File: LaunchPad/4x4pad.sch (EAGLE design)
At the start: 17 parts

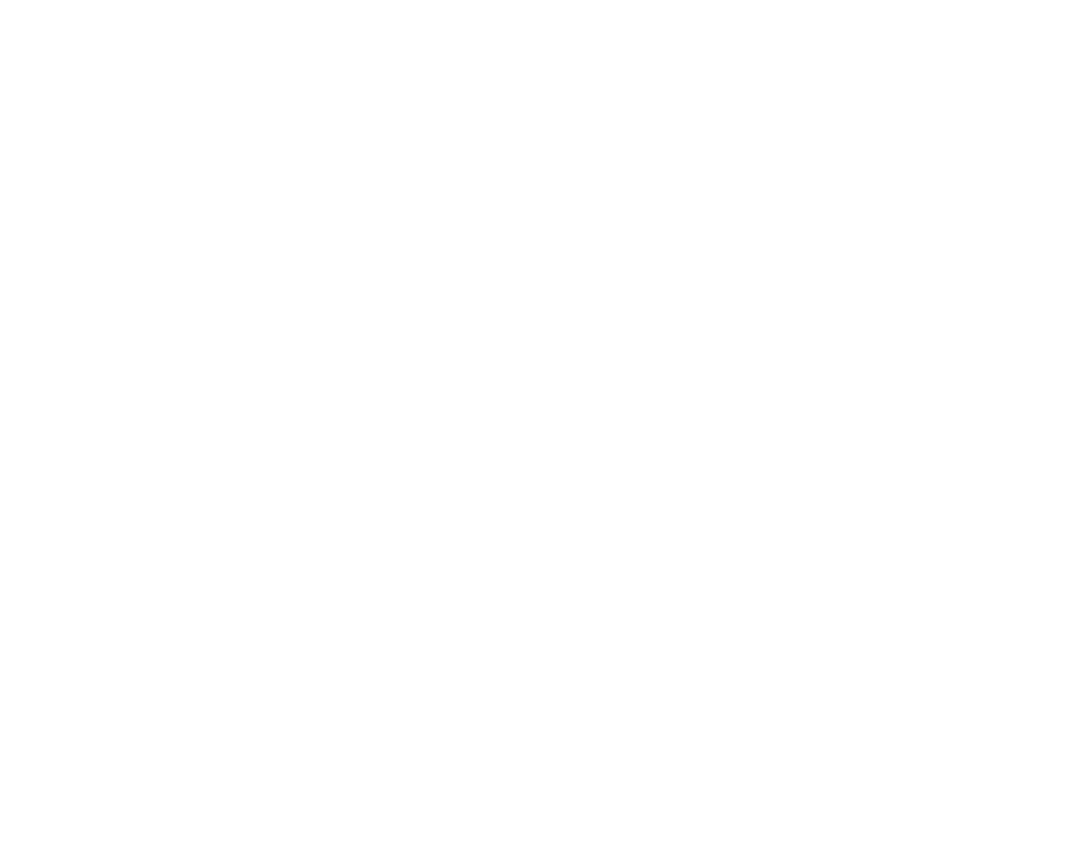
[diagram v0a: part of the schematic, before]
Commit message: Restarted 4x4 board, still need vertical button jumpoers, button connection
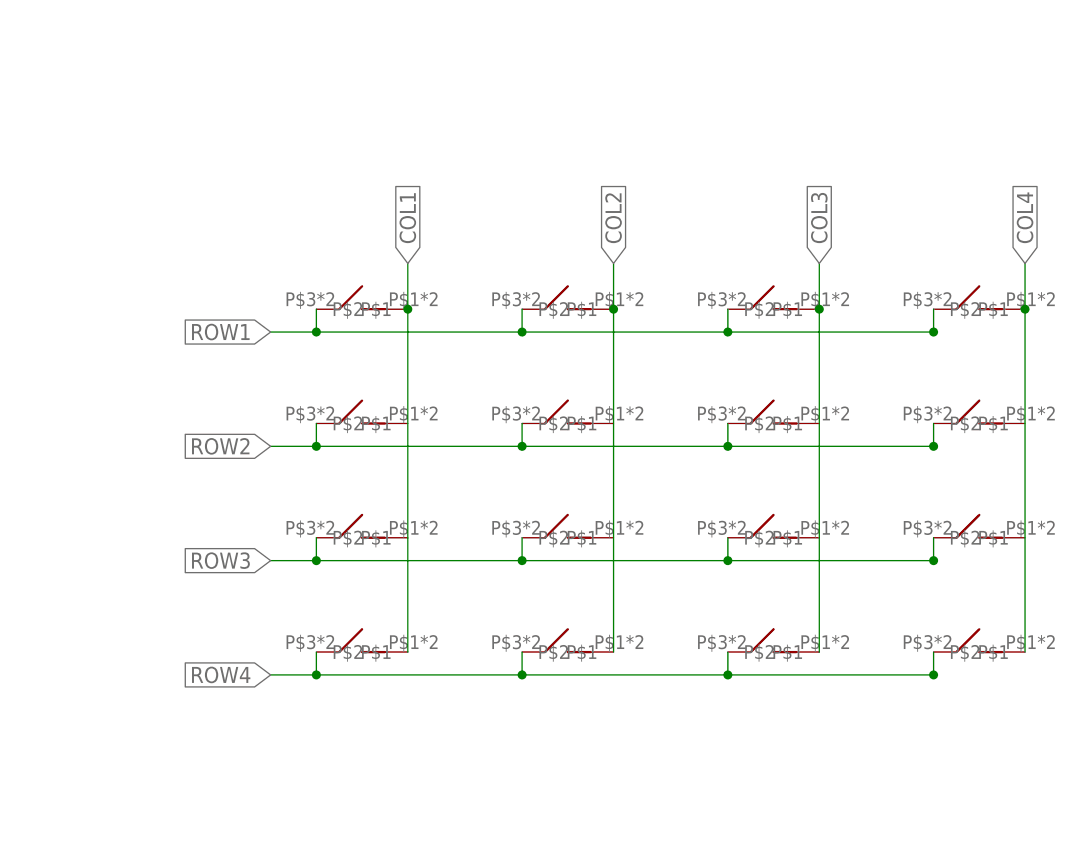
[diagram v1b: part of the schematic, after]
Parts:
- added U$18, U$19, U$20, U$21, U$22, U$23, U$24, U$25, U$26, U$27, U$28, U$29, U$30, U$31, U$32, U$33: SOFT-TACTILE-PUSHBUTTON, launchpadParts:SOFT-TACTILE-PUSHBUTTON
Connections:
- net +5V renamed N$36
- net GND renamed N$37
- new net COL1: U$18.P$2, U$30.P$2
- new net COL2: U$19.P$2, U$31.P$2
- new net COL3: U$20.P$2, U$32.P$2
- new net COL4: U$21.P$2, U$33.P$2
- new net ROW1: U$18.P$1, U$19.P$1, U$20.P$1, U$21.P$1
- new net ROW2: U$22.P$1, U$23.P$1, U$24.P$1, U$25.P$1
- new net ROW3: U$26.P$1, U$27.P$1, U$28.P$1, U$29.P$1
- new net ROW4: U$30.P$1, U$31.P$1, U$32.P$1, U$33.P$1
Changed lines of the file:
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@@
 <part name="P+16" library="supply1" library_urn="urn:adsk.eagle:library:371" deviceset="+5V" device=""/>
 <part name="P+17" library="supply1" library_urn="urn:adsk.eagle:library:371" deviceset="+5V" device=""/>
+<part name="U$18" library="launchpadParts" deviceset="SOFT-TACTILE-PUSHBUTTON" device=""/>
+<part name="U$19" library="launchpadParts" deviceset="SOFT-TACTILE-PUSHBUTTON" device=""/>
+<part name="U$20" library="launchpadParts" deviceset="SOFT-TACTILE-PUSHBUTTON" device=""/>
+<part name="U$21" library="launchpadParts" deviceset="SOFT-TACTILE-PUSHBUTTON" device=""/>
+<part name="U$22" library="launchpadParts" deviceset="SOFT-TACTILE-PUSHBUTTON" device=""/>
+<part name="U$23" library="launchpadParts" deviceset="SOFT-TACTILE-PUSHBUTTON" device=""/>
+<part name="U$24" library="launchpadParts" deviceset="SOFT-TACTILE-PUSHBUTTON" device=""/>
+<part name="U$25" library="launchpadParts" deviceset="SOFT-TACTILE-PUSHBUTTON" device=""/>
+<part name="U$26" library="launchpadParts" deviceset="SOFT-TACTILE-PUSHBUTTON" device=""/>
+<part name="U$27" library="launchpadParts" deviceset="SOFT-TACTILE-PUSHBUTTON" device=""/>
+<part name="U$28" library="launchpadParts" deviceset="SOFT-TACTILE-PUSHBUTTON" device=""/>
+<part name="U$29" library="launchpadParts" deviceset="SOFT-TACTILE-PUSHBUTTON" device=""/>
+<part name="U$30" library="launchpadParts" deviceset="SOFT-TACTILE-PUSHBUTTON" device=""/>
+<part name="U$31" library="launchpadParts" deviceset="SOFT-TACTILE-PUSHBUTTON" device=""/>
+<part name="U$32" library="launchpadParts" deviceset="SOFT-TACTILE-PUSHBUTTON" device=""/>
+<part name="U$33" library="launchpadParts" deviceset="SOFT-TACTILE-PUSHBUTTON" device=""/>
 </parts>
 <sheets>
@@
 <instance part="P+16" gate="1" x="109.22" y="-101.6" rot="R270"/>
 <instance part="P+17" gate="1" x="147.32" y="-101.6" rot="R270"/>
+<instance part="U$18" gate="G$1" x="228.6" y="-15.24"/>
+<instance part="U$19" gate="G$1" x="251.46" y="-15.24"/>
+<instance part="U$20" gate="G$1" x="274.32" y="-15.24"/>
+<instance part="U$21" gate="G$1" x="297.18" y="-15.24"/>
+<instance part="U$22" gate="G$1" x="228.6" y="-27.94"/>
+<instance part="U$23" gate="G$1" x="251.46" y="-27.94"/>
+<instance part="U$24" gate="G$1" x="274.32" y="-27.94"/>
+<instance part="U$25" gate="G$1" x="297.18" y="-27.94"/>
+<instance part="U$26" gate="G$1" x="228.6" y="-40.64"/>
+<instance part="U$27" gate="G$1" x="251.46" y="-40.64"/>
+<instance part="U$28" gate="G$1" x="274.32" y="-40.64"/>
+<instance part="U$29" gate="G$1" x="297.18" y="-40.64"/>
+<instance part="U$30" gate="G$1" x="228.6" y="-53.34"/>
+<instance part="U$31" gate="G$1" x="251.46" y="-53.34"/>
+<instance part="U$32" gate="G$1" x="274.32" y="-53.34"/>
+<instance part="U$33" gate="G$1" x="297.18" y="-53.34"/>
 </instances>
 <busses>
 </busses>
 <nets>
-<net name="+5V" class="0">
+<net name="N$36" class="0">
 <segment>
 <pinref part="U$1" gate="G$1" pin="VCC"/>
@@
 </segment>
 </net>
-<net name="GND" class="0">
+<net name="N$37" class="0">
 <segment>
 <pinref part="U$1" gate="G$1" pin="GND"/>
@@
 </segment>
 </net>
+<net name="COL1" class="0">
+<segment>
+<pinref part="U$18" gate="G$1" pin="P$2"/>
+<pinref part="U$30" gate="G$1" pin="P$2"/>
+<wire x1="233.68" y1="-15.24" x2="233.68" y2="-53.34" width="0.1524" layer="91"/>
+<wire x1="233.68" y1="-15.24" x2="233.68" y2="-10.16" width="0.1524" layer="91"/>
+<junction x="233.68" y="-15.24"/>
+<label x="233.68" y="-10.16" size="1.778" layer="95" rot="R90" xref="yes"/>
+</segment>
+</net>
+<net name="COL2" class="0">
+<segment>
+<pinref part="U$19" gate="G$1" pin="P$2"/>
+<pinref part="U$31" gate="G$1" pin="P$2"/>
+<wire x1="256.54" y1="-15.24" x2="256.54" y2="-53.34" width="0.1524" layer="91"/>
+<wire x1="256.54" y1="-15.24" x2="256.54" y2="-10.16" width="0.1524" layer="91"/>
+<junction x="256.54" y="-15.24"/>
+<label x="256.54" y="-10.16" size="1.778" layer="95" rot="R90" xref="yes"/>
+</segment>
+</net>
+<net name="COL3" class="0">
+<segment>
+<pinref part="U$20" gate="G$1" pin="P$2"/>
+<pinref part="U$32" gate="G$1" pin="P$2"/>
+<wire x1="279.4" y1="-15.24" x2="279.4" y2="-53.34" width="0.1524" layer="91"/>
+<wire x1="279.4" y1="-15.24" x2="279.4" y2="-10.16" width="0.1524" layer="91"/>
+<junction x="279.4" y="-15.24"/>
+<label x="279.4" y="-10.16" size="1.778" layer="95" rot="R90" xref="yes"/>
+</segment>
+</net>
+<net name="COL4" class="0">
+<segment>
+<pinref part="U$21" gate="G$1" pin="P$2"/>
+<pinref part="U$33" gate="G$1" pin="P$2"/>
+<wire x1="302.26" y1="-15.24" x2="302.26" y2="-53.34" width="0.1524" layer="91"/>
+<wire x1="302.26" y1="-15.24" x2="302.26" y2="-10.16" width="0.1524" layer="91"/>
+<junction x="302.26" y="-15.24"/>
+<label x="302.26" y="-10.16" size="1.778" layer="95" rot="R90" xref="yes"/>
+</segment>
+</net>
+<net name="ROW1" class="0">
+<segment>
+<pinref part="U$21" gate="G$1" pin="P$1"/>
+<wire x1="292.1" y1="-15.24" x2="292.1" y2="-17.78" width="0.1524" layer="91"/>
+<wire x1="292.1" y1="-17.78" x2="269.24" y2="-17.78" width="0.1524" layer="91"/>
+<pinref part="U$18" gate="G$1" pin="P$1"/>
+<wire x1="269.24" y1="-17.78" x2="246.38" y2="-17.78" width="0.1524" layer="91"/>
+<wire x1="246.38" y1="-17.78" x2="223.52" y2="-17.78" width="0.1524" layer="91"/>
+<wire x1="218.44" y1="-17.78" x2="223.52" y2="-17.78" width="0.1524" layer="91"/>
+<wire x1="223.52" y1="-17.78" x2="223.52" y2="-15.24" width="0.1524" layer="91"/>
+<pinref part="U$19" gate="G$1" pin="P$1"/>
+<wire x1="246.38" y1="-15.24" x2="246.38" y2="-17.78" width="0.1524" layer="91"/>
+<junction x="246.38" y="-17.78"/>
+<pinref part="U$20" gate="G$1" pin="P$1"/>
+<wire x1="269.24" y1="-15.24" x2="269.24" y2="-17.78" width="0.1524" layer="91"/>
+<junction x="269.24" y="-17.78"/>
+<junction x="223.52" y="-17.78"/>
+<junction x="292.1" y="-17.78"/>
+<label x="218.44" y="-17.78" size="1.778" layer="95" rot="R180" xref="yes"/>
+</segment>
+</net>
+<net name="ROW2" class="0">
+<segment>
+<pinref part="U$25" gate="G$1" pin="P$1"/>
+<wire x1="292.1" y1="-27.94" x2="292.1" y2="-30.48" width="0.1524" layer="91"/>
+<wire x1="292.1" y1="-30.48" x2="269.24" y2="-30.48" width="0.1524" layer="91"/>
+<pinref part="U$22" gate="G$1" pin="P$1"/>
+<wire x1="269.24" y1="-30.48" x2="246.38" y2="-30.48" width="0.1524" layer="91"/>
+<wire x1="246.38" y1="-30.48" x2="223.52" y2="-30.48" width="0.1524" layer="91"/>
+<wire x1="223.52" y1="-30.48" x2="218.44" y2="-30.48" width="0.1524" layer="91"/>
+<wire x1="223.52" y1="-27.94" x2="223.52" y2="-30.48" width="0.1524" layer="91"/>
+<junction x="223.52" y="-30.48"/>
+<pinref part="U$23" gate="G$1" pin="P$1"/>
+<wire x1="246.38" y1="-27.94" x2="246.38" y2="-30.48" width="0.1524" layer="91"/>
+<junction x="246.38" y="-30.48"/>
+<pinref part="U$24" gate="G$1" pin="P$1"/>
+<wire x1="269.24" y1="-27.94" x2="269.24" y2="-30.48" width="0.1524" layer="91"/>
+<junction x="269.24" y="-30.48"/>
+<junction x="292.1" y="-30.48"/>
+<label x="218.44" y="-30.48" size="1.778" layer="95" rot="R180" xref="yes"/>
+</segment>
+</net>
+<net name="ROW3" class="0">
+<segment>
+<pinref part="U$29" gate="G$1" pin="P$1"/>
+<wire x1="292.1" y1="-40.64" x2="292.1" y2="-43.18" width="0.1524" layer="91"/>
+<wire x1="292.1" y1="-43.18" x2="269.24" y2="-43.18" width="0.1524" layer="91"/>
+<pinref part="U$26" gate="G$1" pin="P$1"/>
+<wire x1="269.24" y1="-43.18" x2="246.38" y2="-43.18" width="0.1524" layer="91"/>
+<wire x1="246.38" y1="-43.18" x2="223.52" y2="-43.18" width="0.1524" layer="91"/>
+<wire x1="223.52" y1="-43.18" x2="218.44" y2="-43.18" width="0.1524" layer="91"/>
+<wire x1="223.52" y1="-40.64" x2="223.52" y2="-43.18" width="0.1524" layer="91"/>
+<junction x="223.52" y="-43.18"/>
+<pinref part="U$27" gate="G$1" pin="P$1"/>
+<wire x1="246.38" y1="-40.64" x2="246.38" y2="-43.18" width="0.1524" layer="91"/>
+<junction x="246.38" y="-43.18"/>
+<pinref part="U$28" gate="G$1" pin="P$1"/>
+<wire x1="269.24" y1="-40.64" x2="269.24" y2="-43.18" width="0.1524" layer="91"/>
+<junction x="269.24" y="-43.18"/>
+<junction x="292.1" y="-43.18"/>
+<label x="218.44" y="-43.18" size="1.778" layer="95" rot="R180" xref="yes"/>
+</segment>
+</net>
+<net name="ROW4" class="0">
+<segment>
+<pinref part="U$33" gate="G$1" pin="P$1"/>
+<wire x1="292.1" y1="-53.34" x2="292.1" y2="-55.88" width="0.1524" layer="91"/>
+<wire x1="292.1" y1="-55.88" x2="269.24" y2="-55.88" width="0.1524" layer="91"/>
+<pinref part="U$30" gate="G$1" pin="P$1"/>
+<wire x1="269.24" y1="-55.88" x2="246.38" y2="-55.88" width="0.1524" layer="91"/>
+<wire x1="246.38" y1="-55.88" x2="223.52" y2="-55.88" width="0.1524" layer="91"/>
+<wire x1="223.52" y1="-55.88" x2="218.44" y2="-55.88" width="0.1524" layer="91"/>
+<wire x1="223.52" y1="-53.34" x2="223.52" y2="-55.88" width="0.1524" layer="91"/>
+<pinref part="U$32" gate="G$1" pin="P$1"/>
+<wire x1="269.24" y1="-53.34" x2="269.24" y2="-55.88" width="0.1524" layer="91"/>
+<junction x="269.24" y="-55.88"/>
+<pinref part="U$31" gate="G$1" pin="P$1"/>
+<wire x1="246.38" y1="-53.34" x2="246.38" y2="-55.88" width="0.1524" layer="91"/>
+<junction x="246.38" y="-55.88"/>
+<junction x="292.1" y="-55.88"/>
+<junction x="223.52" y="-55.88"/>
+<label x="218.44" y="-55.88" size="1.778" layer="95" rot="R180" xref="yes"/>
+</segment>
+</net>
